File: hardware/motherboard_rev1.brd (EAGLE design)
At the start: 35.5 x 87 mm, 81 parts, among them CN1 UG-2828GDEDF11-1.5OLED, CN2 1X05, CN3 1X06, CN4 FEMALE, CN6 CON-MOLEX-2MMFEMALE, CN7 CON-MOLEX-2MMFEMALE_RA, CN8 CON-MOLEX-2MMFEMALE_RA, CN9 CON-MOLEX-2MMFEMALE_RA, U1 MCP73831, X1 CRYSTAL-ABM7-8.000MHZ-D-2-Y-T

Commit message: Added revision 1 to motherboard, as well as CHANGELOG file
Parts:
- removed TP1, TP2: TEST-POINT2, SparkFun-Passives:PAD.02X.02
- added R16, R17: 4.7k, notes_mark5a:0603
- CN3: value 1X06 -> PHF-106-01-L-S
- moved CN4 10.3 mm to (74.8, 23.2)
- moved CN2 8.38 mm to (87.5, 46.5)
- moved C30 7.15 mm to (63.2, 38.4), flipped to the bottom
- moved SJ1 6.58 mm to (84.0, 20.2), turned to 90 degrees
- moved C4 5.15 mm to (76.0, 18.8), turned to 0 degrees
- moved R7 4.56 mm to (72.2, 18.8), turned to 0 degrees
- moved C3 4.37 mm to (81.2, 10.8)
- moved C48 4.37 mm to (66.6, 17.9)
- moved CN5 4.37 mm to (58.8, 13.0)
- moved D1 4.37 mm to (67.8, 9.50)
- moved D4 4.37 mm to (77.8, 9.50)
- moved D5 4.37 mm to (75.8, 9.50)
- moved R1 4.37 mm to (77.8, 13.2)
- moved R13 4.37 mm to (69.8, 9.50)
- moved R2 4.37 mm to (75.8, 13.2)
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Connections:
- net 3.3V: now also C1.1, C12.2, C8.2, L1.2, R16.2, R17.2, U$24.5, U$3.16, U$3.62; no longer C12.1, C8.1, TP1.P$1, TP2.P$1, U$3.15, U$3.65
- net GND: now also C12.1, C8.1, U$3.15, U$3.65; no longer C12.2, C8.2, U$3.16, U$3.62
- net SCL1: now also R17.1
- net SDA1: now also R16.1
- net VIN: no longer C1.1, L1.2, U$24.5
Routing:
- net SDA1: track 158.5 -> 171.6 mm
- net SCL1: track 158.5 -> 170.7 mm
- net VIN: track 111.1 -> 99.6 mm
- net 3.3V: track 381.3 -> 392.5 mm
- net N$11: track 5.84 -> 16.5 mm
- net AN8: track 42.3 -> 52.5 mm
- net AN12: track 46.0 -> 56.1 mm
- net IO82/TOUCH_INT: track 51.6 -> 61.8 mm
- net PGEC2: track 8.28 -> 17.1 mm
- net IO53/CC3000_CS: track 49.6 -> 55.9 mm
- net PGED2: track 13.8 -> 20.1 mm
- net MCLR#: track 69.3 -> 63.6 mm
- net IO7/RAD_SIG1: track 51.8 -> 57.2 mm
- net IO9/AUDIO: track 28.8 -> 34.2 mm
- net SPI_CLK: track 49.8 -> 54.7 mm
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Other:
- board size 35.5 x 87 mm -> 39.5 x 91 mm
- board text added: "rev1"
- board text removed: "rev0"

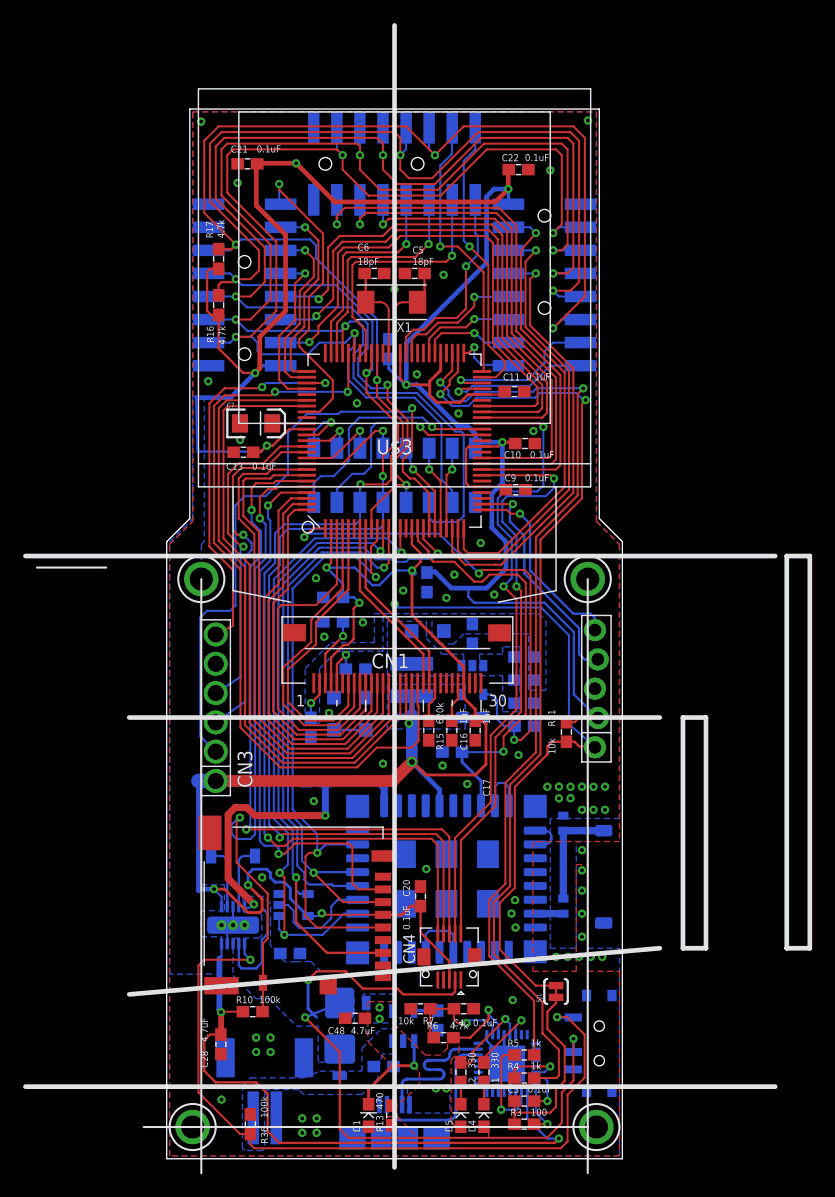
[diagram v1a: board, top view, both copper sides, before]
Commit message: Added motherboard rev1 and capacitive touch board rev2
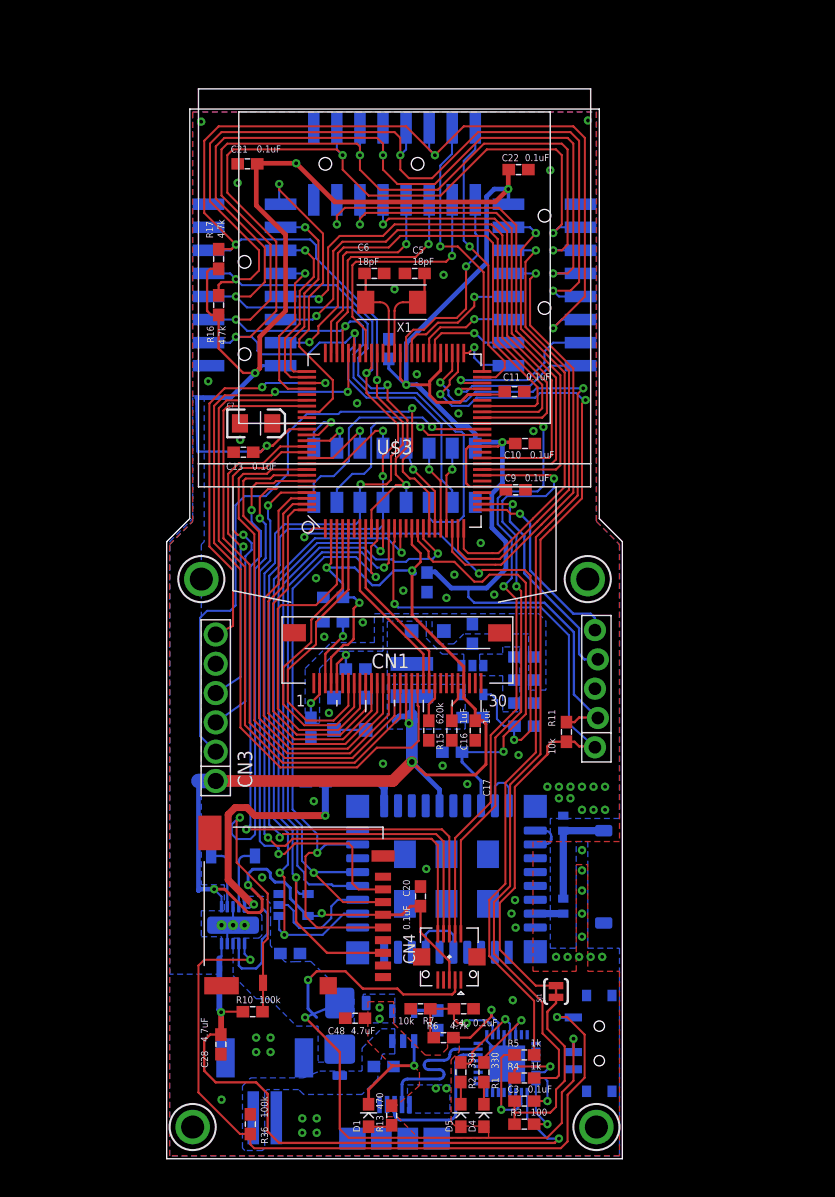
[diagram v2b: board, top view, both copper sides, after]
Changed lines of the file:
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@@
 <setting verticaltext="up"/>
 </settings>
-<grid distance="0.125" unitdist="mm" unit="mm" style="lines" multiple="1" display="yes" altdistance="0.025" altunitdist="inch" altunit="inch"/>
+<grid distance="0.25" unitdist="mm" unit="mm" style="lines" multiple="1" display="yes" altdistance="0.025" altunitdist="inch" altunit="inch"/>
 <layers>
 <layer number="1" name="Top" color="4" fill="1" visible="yes" active="yes"/>
@@
 <layer number="20" name="Dimension" color="15" fill="1" visible="yes" active="yes"/>
 <layer number="21" name="tPlace" color="7" fill="1" visible="yes" active="yes"/>
-<layer number="22" name="bPlace" color="7" fill="1" visible="no" active="yes"/>
+<layer number="22" name="bPlace" color="7" fill="1" visible="yes" active="yes"/>
 <layer number="23" name="tOrigins" color="15" fill="1" visible="yes" active="yes"/>
-<layer number="24" name="bOrigins" color="15" fill="1" visible="no" active="yes"/>
-<layer number="25" name="tNames" color="7" fill="1" visible="yes" active="yes"/>
-<layer number="26" name="bNames" color="7" fill="1" visible="no" active="yes"/>
-<layer number="27" name="tValues" color="7" fill="1" visible="yes" active="yes"/>
+<layer number="24" name="bOrigins" color="15" fill="1" visible="yes" active="yes"/>
+<layer number="25" name="tNames" color="7" fill="1" visible="no" active="yes"/>
+<layer number="26" name="bNames" color="7" fill="1" visible="yes" active="yes"/>
+<layer number="27" name="tValues" color="7" fill="1" visible="no" active="yes"/>
 <layer number="28" name="bValues" color="7" fill="1" visible="no" active="yes"/>
 <layer number="29" name="tStop" color="7" fill="3" visible="no" active="yes"/>
@@
 <text x="60.5" y="92.75" size="1.016" layer="22" rot="MR0">Mini</text>
 <text x="60.5" y="91.25" size="1.016" layer="22" rot="MR0">rev1</text>
-<text x="51.25" y="36.5" size="1.016" layer="22" rot="MR90">make | share | dream | give</text>
+<text x="51.25" y="30" size="1.016" layer="22" rot="MR90">make | share | dream | give</text>
 <wire x1="68.625" y1="79.875" x2="71.375" y2="79.875" width="0.2032" layer="22" curve="-247.380135"/>
 <wire x1="71.375" y1="79.875" x2="71.875" y2="78.625" width="0.2032" layer="22"/>
@@
 <wire x1="67" y1="79.75" x2="66.75" y2="80.75" width="0.2032" layer="22" curve="-18.717192"/>
 <text x="71.625" y="78" size="1.016" layer="22" rot="MR0">OSH</text>
-<wire x1="103" y1="58" x2="38" y2="58" width="0.4064" layer="21"/>
-<wire x1="103" y1="12" x2="38" y2="12" width="0.4064" layer="21"/>
-<wire x1="70" y1="5" x2="70" y2="104" width="0.4064" layer="21"/>
-<wire x1="93" y1="24" x2="47" y2="20" width="0.4064" layer="21"/>
-<wire x1="47" y1="44" x2="93" y2="44" width="0.4064" layer="21"/>
-<wire x1="104" y1="58" x2="104" y2="24" width="0.4064" layer="21"/>
-<wire x1="104" y1="24" x2="106" y2="24" width="0.4064" layer="21"/>
-<wire x1="106" y1="24" x2="106" y2="58" width="0.4064" layer="21"/>
-<wire x1="106" y1="58" x2="104" y2="58" width="0.4064" layer="21"/>
-<wire x1="95" y1="44" x2="95" y2="24" width="0.4064" layer="21"/>
-<wire x1="95" y1="24" x2="97" y2="24" width="0.4064" layer="21"/>
-<wire x1="97" y1="24" x2="97" y2="44" width="0.4064" layer="21"/>
-<wire x1="97" y1="44" x2="95" y2="44" width="0.4064" layer="21"/>
-<wire x1="45" y1="57" x2="39" y2="57" width="0.1778" layer="21"/>
 <circle x="53.25" y="56" radius="2" width="0.1778" layer="21"/>
 <circle x="53.5" y="56" radius="2.25" width="0.1778" layer="42"/>
@@
 <circle x="86.75" y="56" radius="2" width="0.1778" layer="21"/>
 <circle x="86.75" y="56" radius="2.06155" width="0.1778" layer="22"/>
-<wire x1="53.25" y1="56" x2="53.25" y2="4.5" width="0.1778" layer="21"/>
-<wire x1="86.75" y1="56" x2="86.75" y2="8.5" width="0.1778" layer="21"/>
 <circle x="87.5" y="8.5" radius="2" width="0.1778" layer="21"/>
-<wire x1="86.75" y1="8.5" x2="86.75" y2="4.5" width="0.1778" layer="21"/>
-<wire x1="86.75" y1="8.5" x2="48.25" y2="8.5" width="0.1778" layer="21"/>
 <circle x="52.5" y="8.5" radius="2" width="0.1778" layer="21"/>
 <circle x="87.5" y="8.5" radius="2.06155" width="0.1778" layer="22"/>
 <circle x="52.5" y="8.5" radius="2.06155" width="0.1778" layer="22"/>
+<wire x1="74.75" y1="23.375" x2="74.75" y2="23.125" width="0.1778" layer="21"/>
+<wire x1="74.625" y1="23.25" x2="74.875" y2="23.25" width="0.1778" layer="21"/>
 </plain>
 <attributes>
@@
 <via x="68.7044" y="18.86" extent="1-16" drill="0.3302"/>
 <via x="68.7044" y="17.8828" extent="1-16" drill="0.3302"/>
-<wire x1="79" y1="16.5" x2="79" y2="17.4036" width="0.2032" layer="16"/>
-<wire x1="79" y1="17.4036" x2="78.1532" y2="18.2504" width="0.2032" layer="16"/>
-<wire x1="78.1532" y1="18.2504" x2="78.1532" y2="18.6568" width="0.2032" layer="16"/>
-<via x="78.1532" y="18.6568" extent="1-16" drill="0.3302"/>
-<wire x1="78.1532" y1="18.6568" x2="78.1532" y2="17.836" width="0.2032" layer="1"/>
-<wire x1="78.1532" y1="17.836" x2="76.5672" y2="16.25" width="0.2032" layer="1"/>
+<wire x1="79" y1="16.5" x2="79" y2="17.5286" width="0.2032" layer="16"/>
+<wire x1="79" y1="17.5286" x2="78.4032" y2="18.1254" width="0.2032" layer="16"/>
+<wire x1="78.4032" y1="18.1254" x2="78.4032" y2="18.6568" width="0.2032" layer="16"/>
+<via x="78.4032" y="18.6568" extent="1-16" drill="0.3302"/>
+<wire x1="78.4032" y1="18.6568" x2="78.4032" y2="18.086" width="0.2032" layer="1"/>
+<wire x1="78.4032" y1="18.086" x2="76.5672" y2="16.25" width="0.2032" layer="1"/>
 <wire x1="76.5672" y1="16.25" x2="75.1" y2="16.25" width="0.2032" layer="1"/>
 </signal>
@@
 <wire x1="57.408" y1="27.5" x2="57.8104" y2="27.8008" width="0.1778" layer="16"/>
 <via x="57.8104" y="27.8008" extent="1-16" drill="0.3302"/>
-<wire x1="57.8104" y1="27.8008" x2="55.5752" y2="30.036" width="0.6096" layer="1"/>
-<wire x1="55.5752" y1="30.036" x2="55.5752" y2="35.5852" width="0.6096" layer="1"/>
+<wire x1="55.5752" y1="29.9248" x2="55.5752" y2="35.5852" width="0.6096" layer="1"/>
 <wire x1="55.5752" y1="35.5852" x2="56.1848" y2="36.1948" width="0.6096" layer="1"/>
 <wire x1="56.1848" y1="36.1948" x2="57.2008" y2="36.1948" width="0.6096" layer="1"/>
@@
 <wire x1="75" y1="20" x2="75.25" y2="20.25" width="0.2032" layer="1"/>
 <wire x1="75.25" y1="20.25" x2="75.25" y2="21.25" width="0.2032" layer="1"/>
+<wire x1="55.5752" y1="29.9248" x2="57.6992" y2="27.8008" width="0.6096" layer="1"/>
+<wire x1="57.6992" y1="27.8008" x2="57.8104" y2="27.8008" width="0.6096" layer="1"/>
 </signal>
 <signal name="EN_REG">
